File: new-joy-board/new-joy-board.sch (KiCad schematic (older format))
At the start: 28 parts, among them J0 SDS-50J, J1 SDS-50J, J2 SDS-50J, J3 SDS-50J, J4 BAT, U0 P82B715, U1 P82B715, U10 oskj-dc-dc, U2 P82B715, U3 P82B715, U4 AZReady_ESP32, U7 MPU6050_Breakout

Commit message: First draft of full layout
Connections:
- wire segments 47 -> 60
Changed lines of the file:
@@
 Wire Wire Line
 	7150 1500 7500 1500
+Wire Wire Line
+	1700 3350 1700 3150
+Wire Wire Line
+	1700 3150 1850 3150
+Wire Wire Line
+	1850 3150 1850 3950
+Wire Wire Line
+	1850 3950 1700 3950
+Connection ~ 1700 3950
+Wire Wire Line
+	1700 4250 1850 4250
+Wire Wire Line
+	1850 4250 1850 4850
+Wire Wire Line
+	1850 4850 1700 4850
+Connection ~ 1700 4850
+Wire Wire Line
+	1700 5150 1850 5150
+Wire Wire Line
+	1850 5150 1850 5750
+Wire Wire Line
+	1850 5750 1700 5750
+Connection ~ 1700 5750
+Wire Wire Line
+	1700 6050 1850 6050
+Wire Wire Line
+	1850 6050 1850 6650
+Wire Wire Line
+	1850 6650 1700 6650
+Connection ~ 1700 6650
 $EndSCHEMATC

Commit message: Start rework to slimmer design, and add capacitors to I2C drivers
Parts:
- added C1, C2, C3, C4: 0.1uF, Capacitor_SMD:C_0805_2012Metric_Pad1.15x1.40mm_HandSolder, symbol Device:C
- added C5, C6, C7, C8: 1uF, Capacitor_SMD:C_0805_2012Metric_Pad1.15x1.40mm_HandSolder, symbol Device:C
- R1, R10, R11, R12, R13, R14, R15, R16, R2, R3, R4, R5, R6, R7, R8, R9: footprint Resistor_SMD:R_1210_3225Metric_Pad1.42x2.65mm_HandSolder -> Resistor_SMD:R_0805_2012Metric_Pad1.15x1.40mm_HandSolder
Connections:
- wire segments 60 -> 84

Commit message: Route new board layout
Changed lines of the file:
@@
 $EndComp
 Text Label 4600 4200 0    60   ~ 0
-SDA0ESP
+SCL1ESP
 Text Label 4600 4100 0    60   ~ 0
-SCL0ESP
+SDA1ESP
 $Comp
 L new-joy-board-rescue:R R1
@@
 $EndComp
 Text Label 9250 5350 0    60   ~ 0
-SCL0ESP
+SCL3ESP
 Text Label 9250 5450 0    60   ~ 0
-SDA0ESP
+SDA3ESP
 $Comp
 L power:+3.3V #PWR013
@@
 	5050 3900 4600 3900
 Text Label 4600 3900 0    50   ~ 0
-SCL1ESP
+SDA0ESP
 Text Label 4600 4000 0    50   ~ 0
-SDA1ESP
+SCL0ESP
 Wire Wire Line
 	6200 4100 6500 4100
@@
 	6200 4300 6500 4300
 Text Label 6500 4100 2    50   ~ 0
+SDA3ESP
+Text Label 6500 4000 2    50   ~ 0
+SCL3ESP
+Text Label 6500 4200 2    50   ~ 0
 SCL2ESP
-Text Label 6500 4000 2    50   ~ 0
+Text Label 6500 4300 2    50   ~ 0
 SDA2ESP
-Text Label 6500 4200 2    50   ~ 0
-SDA3ESP
-Text Label 6500 4300 2    50   ~ 0
-SCL3ESP
 $Comp
 L new-joy-board-rescue:R R2

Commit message: Designed in the 24L01 board for emergency use
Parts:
- added U5: 24L01, new-joy:24L01, symbol new-joy:24L01
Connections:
- net labels added: CE, CLK, CS0, IRQ, MISO, MOSI
- wire segments 84 -> 96
- no-connect marks 43 -> 37
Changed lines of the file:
@@
 NoConn ~ 5050 3200
 NoConn ~ 5050 3100
-NoConn ~ 6200 3100
-NoConn ~ 6200 3200
 NoConn ~ 6200 3400
-NoConn ~ 6200 3500
-NoConn ~ 6200 3700
-NoConn ~ 6200 3800
 NoConn ~ 6200 4400
 NoConn ~ 6200 4500
@@
 	1    0    0    -1
 $EndComp
-NoConn ~ 6200 3900
 $Comp
 L new-joy:AZReady_ESP32 U4
@@
 Wire Wire Line
 	2250 4250 2250 4450
+Text Label 6500 3100 2    50   ~ 0
+MOSI
+Text Label 6500 3800 2    50   ~ 0
+CLK
+Text Label 6500 3200 2    50   ~ 0
+MISO
+Text Label 6500 3900 2    50   ~ 0
+CS0
+$Comp
+L new-joy:24L01 U5
+U 1 1 5B9D26D1
+P 8450 3550
+F 0 "U5" H 8700 3600 50  0000 C CNN
+F 1 "24L01" H 8450 3600 50  0000 C CNN
+F 2 "new-joy:24L01" H 9100 4100 50  0001 C CNN
+F 3 "" H 8450 3550 50  0001 C CNN
+	1    8450 3550
+	1    0    0    -1
+$EndComp
+Text Label 6500 3700 2    50   ~ 0
+CE
+Wire Wire Line
+	6200 3500 6500 3500
+Text Label 6500 3500 2    50   ~ 0
+IRQ
+Wire Wire Line
+	6200 3200 6500 3200
+Wire Wire Line
+	6200 3100 6500 3100
+Wire Wire Line
+	6200 3700 6500 3700
+Wire Wire Line
+	6200 3800 6500 3800
+Wire Wire Line
+	6200 3900 6500 3900
+Wire Wire Line
+	7850 3350 7600 3350
+Wire Wire Line
+	7850 3450 7600 3450
+Wire Wire Line
+	7600 3550 7850 3550
+Wire Wire Line
+	7850 3650 7600 3650
+Wire Wire Line
+	9050 3650 9300 3650
+Wire Wire Line
+	9050 3350 9300 3350
+Text Label 7600 3350 0    50   ~ 0
+CS0
+Text Label 7600 3450 0    50   ~ 0
+MOSI
+Text Label 7600 3550 0    50   ~ 0
+MISO
+Text Label 7600 3650 0    50   ~ 0
+CLK
+Text Label 9300 3350 2    50   ~ 0
+IRQ
+Text Label 9300 3650 2    50   ~ 0
+CE
+$Comp
+L power:GND #PWR016
+U 1 1 5B9EFC7D
+P 8450 3950
+F 0 "#PWR016" H 8450 3700 50  0001 C CNN
+F 1 "GND" H 8455 3777 50  0000 C CNN
+F 2 "" H 8450 3950 50  0001 C CNN
+F 3 "" H 8450 3950 50  0001 C CNN
+	1    8450 3950
+	1    0    0    -1
+$EndComp
+$Comp
+L power:+3.3V #PWR015
+U 1 1 5B9EFD23
+P 8450 3100
+F 0 "#PWR015" H 8450 2950 50  0001 C CNN
+F 1 "+3.3V" H 8465 3273 50  0000 C CNN
+F 2 "" H 8450 3100 50  0001 C CNN
+F 3 "" H 8450 3100 50  0001 C CNN
+	1    8450 3100
+	1    0    0    -1
+$EndComp
 $EndSCHEMATC

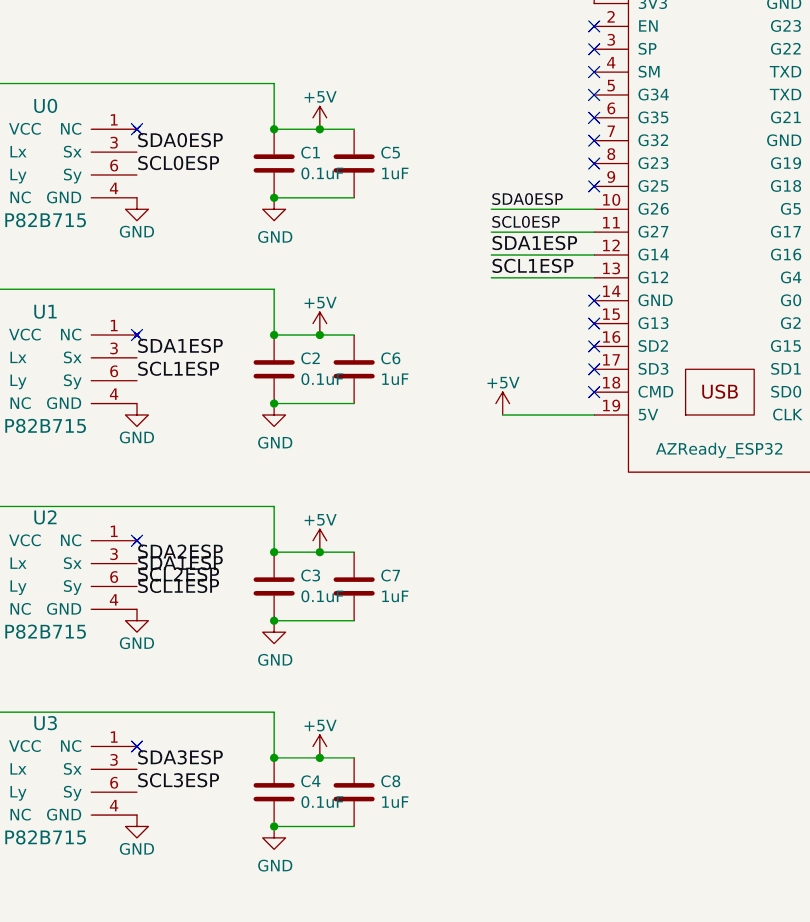
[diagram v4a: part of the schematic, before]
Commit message: Replaced the 1uF with 47uF Elekos as per David's recommendation
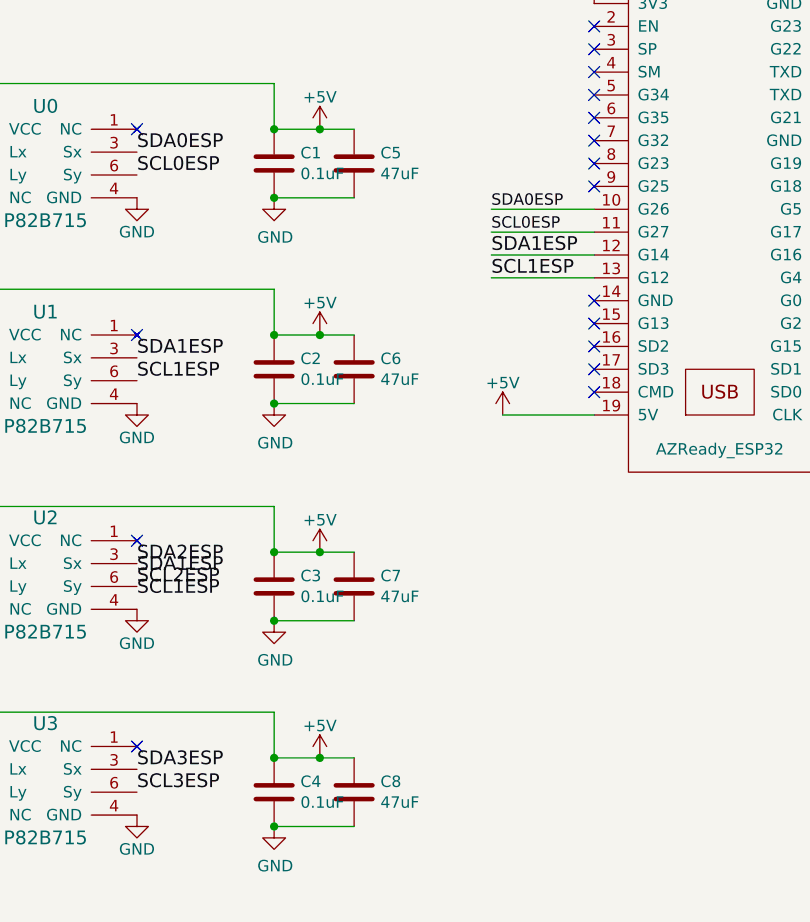
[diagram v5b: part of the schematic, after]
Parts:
- C5, C6, C7, C8: value 1uF -> 47uF; footprint Capacitor_SMD:C_0805_2012Metric_Pad1.15x1.40mm_HandSolder -> Capacitor_SMD:CP_Elec_5x5.8
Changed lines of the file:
@@
 P 4000 3700
 F 0 "C5" H 4115 3746 50  0000 L CNN
-F 1 "1uF" H 4115 3655 50  0000 L CNN
-F 2 "Capacitor_SMD:C_0805_2012Metric_Pad1.15x1.40mm_HandSolder" H 4038 3550 50  0001 C CNN
+F 1 "47uF" H 4115 3655 50  0000 L CNN
+F 2 "Capacitor_SMD:CP_Elec_5x5.8" H 4038 3550 50  0001 C CNN
 F 3 "~" H 4000 3700 50  0001 C CNN
 	1    4000 3700
@@
 P 4000 4600
 F 0 "C6" H 4115 4646 50  0000 L CNN
-F 1 "1uF" H 4115 4555 50  0000 L CNN
-F 2 "Capacitor_SMD:C_0805_2012Metric_Pad1.15x1.40mm_HandSolder" H 4038 4450 50  0001 C CNN
+F 1 "47uF" H 4115 4555 50  0000 L CNN
+F 2 "Capacitor_SMD:CP_Elec_5x5.8" H 4038 4450 50  0001 C CNN
 F 3 "~" H 4000 4600 50  0001 C CNN
 	1    4000 4600
@@
 P 4000 5550
 F 0 "C7" H 4115 5596 50  0000 L CNN
-F 1 "1uF" H 4115 5505 50  0000 L CNN
-F 2 "Capacitor_SMD:C_0805_2012Metric_Pad1.15x1.40mm_HandSolder" H 4038 5400 50  0001 C CNN
+F 1 "47uF" H 4115 5505 50  0000 L CNN
+F 2 "Capacitor_SMD:CP_Elec_5x5.8" H 4038 5400 50  0001 C CNN
 F 3 "~" H 4000 5550 50  0001 C CNN
 	1    4000 5550
@@
 P 4000 6450
 F 0 "C8" H 4115 6496 50  0000 L CNN
-F 1 "1uF" H 4115 6405 50  0000 L CNN
-F 2 "Capacitor_SMD:C_0805_2012Metric_Pad1.15x1.40mm_HandSolder" H 4038 6300 50  0001 C CNN
+F 1 "47uF" H 4115 6405 50  0000 L CNN
+F 2 "Capacitor_SMD:CP_Elec_5x5.8" H 4038 6300 50  0001 C CNN
 F 3 "~" H 4000 6450 50  0001 C CNN
 	1    4000 6450
